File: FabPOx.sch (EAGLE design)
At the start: 37 parts, among them IC1 ATTINY44-SSU, IC2 OPAMPSO08, Q1 TRANSISTOR_PNPSMD, Q2 TRANSISTOR_PNPSMD, U1 HC_05

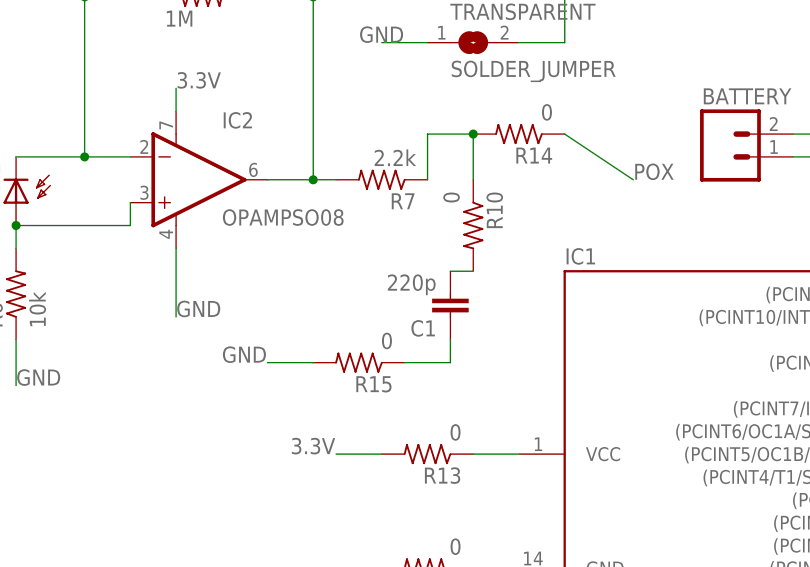
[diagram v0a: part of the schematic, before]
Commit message: Fixed value on capacitor C1
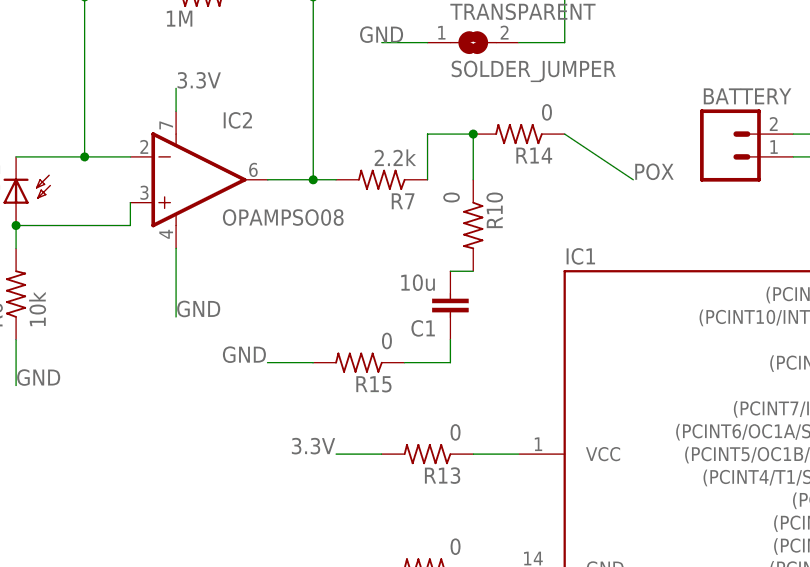
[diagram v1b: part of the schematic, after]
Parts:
- C1: value 220p -> 10u
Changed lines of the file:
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@@
 <part name="R12" library="fab" deviceset="RES-US" device="1206" value="0"/>
 <part name="R13" library="fab" deviceset="RES-US" device="1206" value="0"/>
-<part name="C1" library="SparkFun-Capacitors" deviceset="CAP" device="1206" value="220p"/>
+<part name="C1" library="SparkFun-Capacitors" deviceset="CAP" device="1206" value="10u"/>
 <part name="R10" library="fab" deviceset="RES-US" device="1206" value="0"/>
 <part name="R15" library="fab" deviceset="RES-US" device="1206" value="0"/>
